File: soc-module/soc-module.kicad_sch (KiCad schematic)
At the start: 19 parts, among them J1 Micro_SD, J2 East, J3 West, SW1 Prog, SW2 Reset, U1 ATECC608A-SSHDA, U2 ESP32-WROVER-IE-16MB

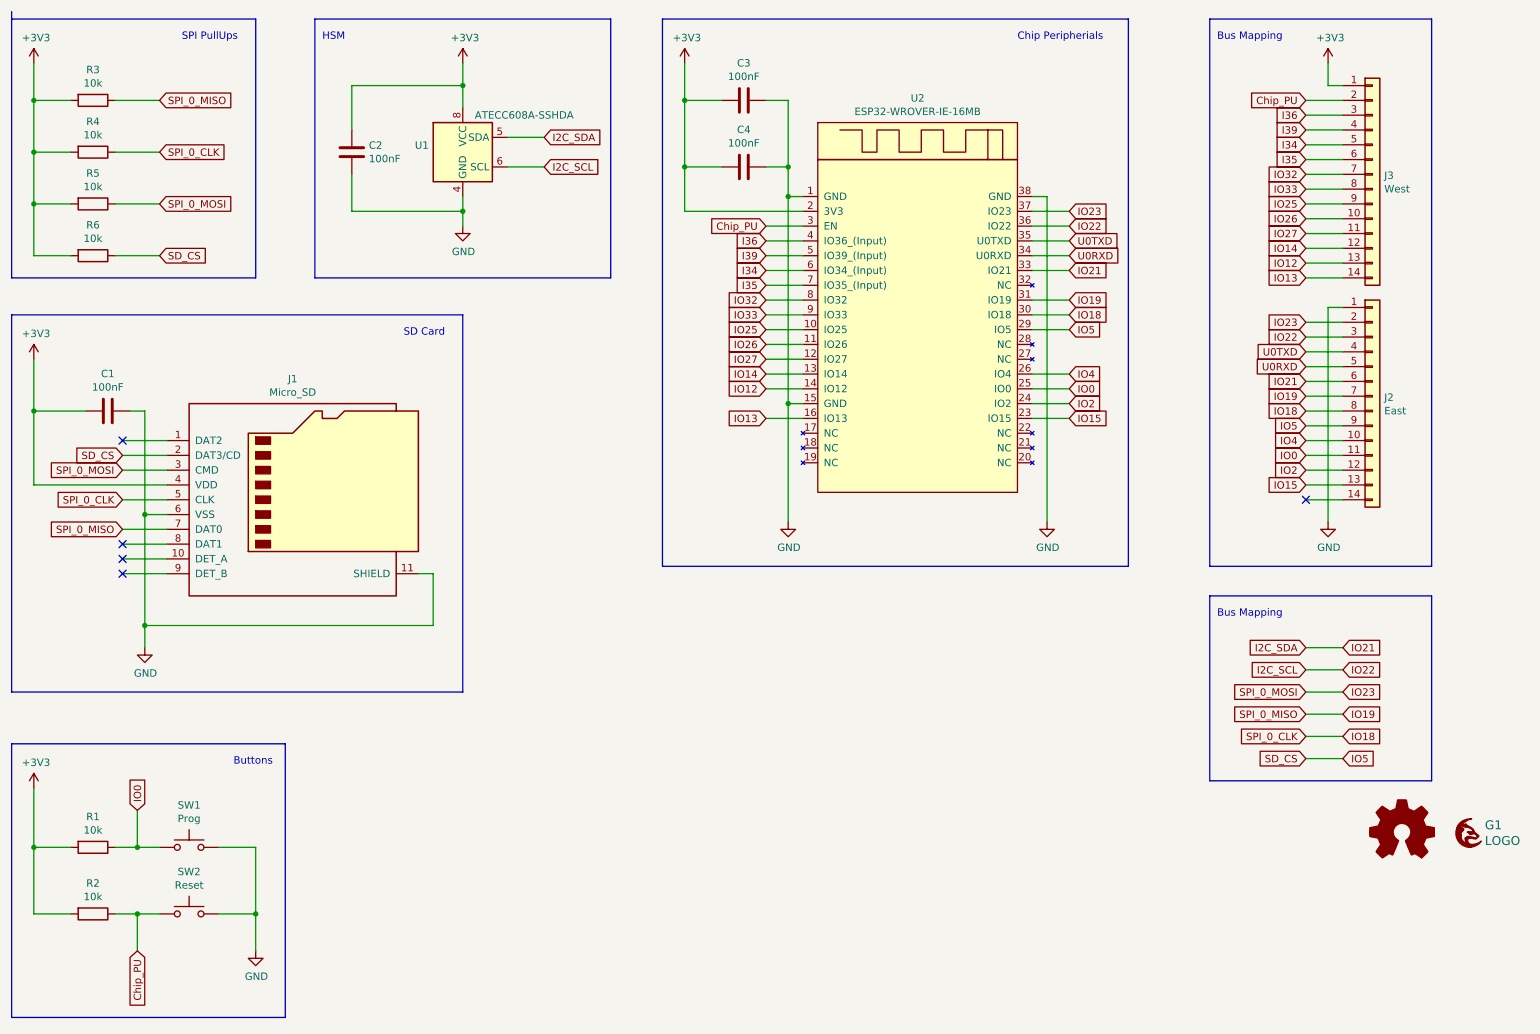
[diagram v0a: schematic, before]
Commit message: Trim further warnings and errors
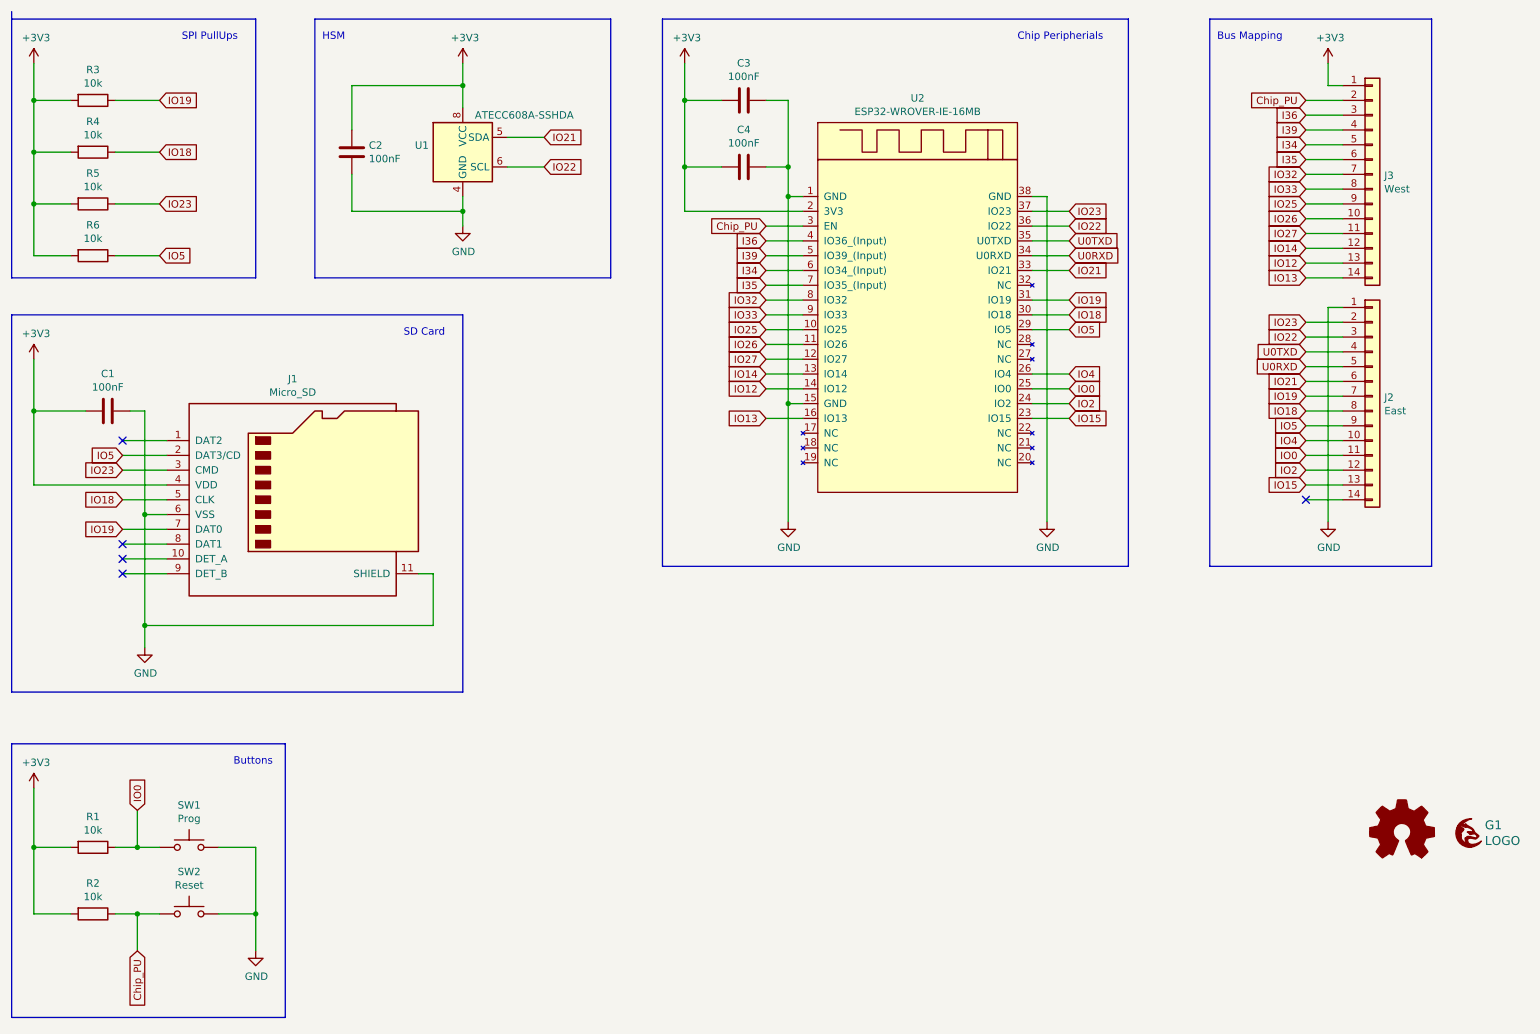
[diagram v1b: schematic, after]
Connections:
- net I2C_SCL renamed IO22
- net I2C_SDA renamed IO21
